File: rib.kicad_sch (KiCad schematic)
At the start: 92 parts, among them J1 RJ45_LED, J10 Conn_01x04_Male, J11 Screw_Terminal_01x02, J12 Screw_Terminal_01x02, J13 Screw_Terminal_01x02, J14 Conn_01x02_Male, J15 Conn_01x02_Male, J16 Conn_01x06_Male, J2 RJ45_LED, J3 RJ45_LED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

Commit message: Fix xbee connection visuals
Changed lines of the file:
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@@
-    (stroke (width 0) (type default))
-  )
-  (wire (pts (xy 289.56 44.45) (xy 326.39 44.45))
     (stroke (width 0) (type default))
   )
@@
   )
   (wire (pts (xy 129.54 246.38) (xy 129.54 248.92))
-    (stroke (width 0) (type default))
-  )
-  (wire (pts (xy 289.56 67.31) (xy 326.39 67.31))
     (stroke (width 0) (type default))
   )
@@
     )
   )
-  (global_label "3.3V" (shape input) (at 326.39 44.45 180) (fields_autoplaced)
-    (effects (font (size 1.27 1.27)) (justify right))
-    (property "Intersheetrefs" "${INTERSHEET_REFS}" (at 319.8645 44.3706 0)
+  (global_label "3.3V" (shape input) (at 289.56 44.45 180) (fields_autoplaced)
+    (effects (font (size 1.27 1.27)) (justify right))
+    (property "Intersheetrefs" "${INTERSHEET_REFS}" (at 283.0345 44.3706 0)
       (effects (font (size 1.27 1.27)) (justify right) hide)
     )
@@
     )
   )
-  (symbol (lib_id "power:GND") (at 326.39 67.31 270) (unit 1)
+  (symbol (lib_id "power:GND") (at 289.56 67.31 270) (unit 1)
     (in_bom yes) (on_board yes) (dnp no)
-    (property "Reference" "#PWR0138" (at 320.04 67.31 0)
-      (effects (font (size 1.27 1.27)) hide)
-    )
-    (property "Value" "GND" (at 318.77 67.31 90)
+    (property "Reference" "#PWR0138" (at 283.21 67.31 0)
+      (effects (font (size 1.27 1.27)) hide)
+    )
+    (property "Value" "GND" (at 281.94 67.31 90)
       (effects (font (size 1.27 1.27)) (justify left))
     )
-    (property "Footprint" "" (at 326.39 67.31 0)
-      (effects (font (size 1.27 1.27)) hide)
-    )
-    (property "Datasheet" "" (at 326.39 67.31 0)
-      (effects (font (size 1.27 1.27)) hide)
-    )
+    (property "Footprint" "" (at 289.56 67.31 0)
+      (effects (font (size 1.27 1.27)) hide)
+    )
+    (property "Datasheet" "" (at 289.56 67.31 0)
+      (effects (font (size 1.27 1.27)) hide)
+    )

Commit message: Fix issues with RC1 - LED orientation, pullups, 3v3 source
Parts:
- added C8: 33uF, Capacitor_THT:CP_Radial_D5.0mm_P2.50mm, symbol Device:C_Polarized
- added U10: LM3940IT-3.3, Package_TO_SOT_THT:TO-220-3_Vertical, symbol LM3940:LM3940IT-3.3
- RN1: value R_Network06 -> 10k_Network06; R 10k -> (none)
- RN2, RN3, RN4: value R_Network05 -> 2k_Network05; R 2k -> (none)
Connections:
- net 3.3V: now also R38.2, R39.2, C8.1, U10.3 (OUT); no longer U1.36 (3V3)
- net 5V: now also R37.1, U10.1 (IN)
- net CATHODE3: now also J1.11, J1.9, J2.11, J2.9, J3.11, J3.9, J4.11, J4.9; no longer J1.10, J1.12, J2.10, J2.12, J3.10, J3.12, J4.10, J4.12
- net GND: now also C8.2, U10.2 (GND); no longer R37.1, R38.2, R39.2
- net LED1: now also J1.12; no longer J1.11
- net LED2: now also J1.10; no longer J1.9
- net LED3: now also J2.12; no longer J2.11
- net LED4: now also J2.10; no longer J2.9
- net LED5: now also J3.12; no longer J3.11
- net LED6: now also J3.10; no longer J3.9
- net LED7: now also J4.12; no longer J4.11
- net LED8: now also J4.10; no longer J4.9
- net MOSFET1: now reaches D6.2 (A), J12.2 (Pin_2), Q1.2 (D)
- net MOSFET2: now reaches D7.2 (A), J13.2 (Pin_2), Q2.2 (D)
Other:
- note removed: "Pullup and enable after not floating"

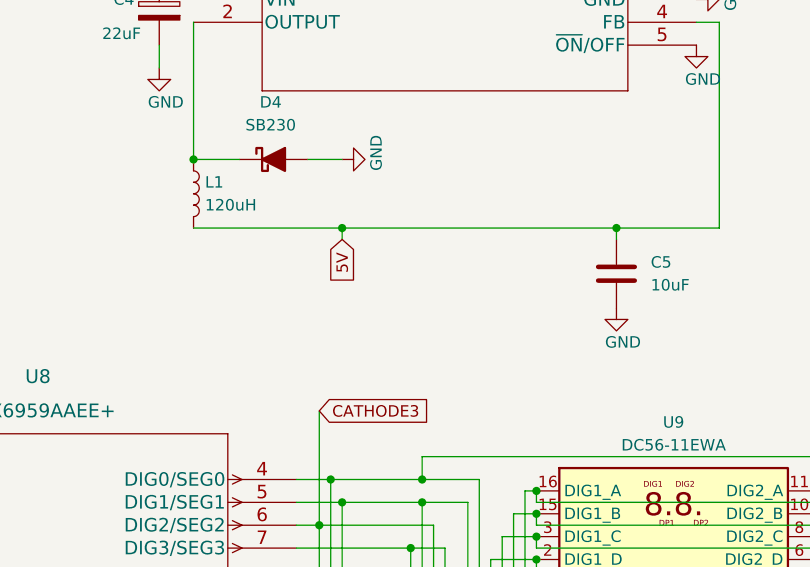
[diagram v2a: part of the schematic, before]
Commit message: prepare to add zener diode
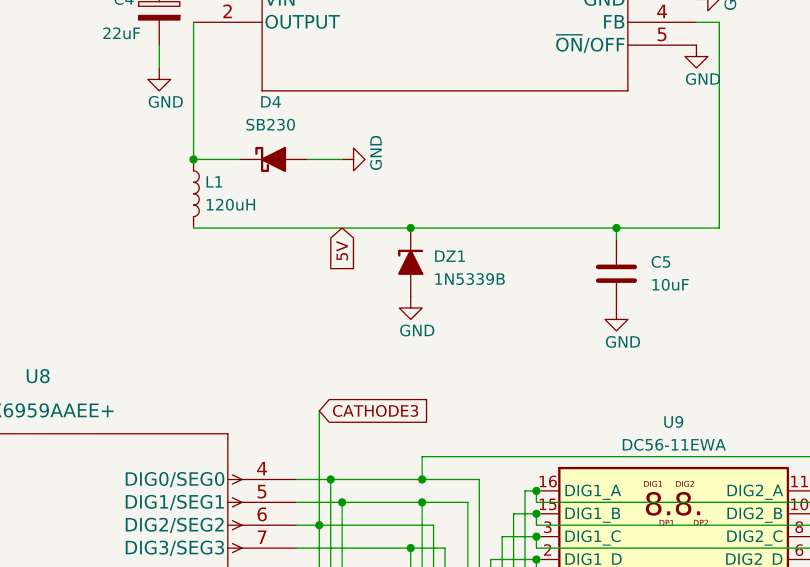
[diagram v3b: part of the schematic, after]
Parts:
- added DZ1: 1N5339B, Diode_THT_AKL:D_5W_CASE-017AA_P12.70mm_Horizontal_Zener, symbol Diode_Zener_AKL:1N5339B
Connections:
- net 5V: now also DZ1.1 (K)
- net GND: now also DZ1.2 (A)
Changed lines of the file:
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@@
   (junction (at 358.14 177.8) (diameter 0) (color 0 0 0 0)
   )
-  (junction (at 351.79 118.11) (diameter 0) (color 0 0 0 0)
-  )
   (junction (at 373.38 147.32) (diameter 0) (color 0 0 0 0)
   )
@@
   (junction (at 355.6 168.91) (diameter 0) (color 0 0 0 0)
   )
+  (junction (at 359.41 118.11) (diameter 0) (color 0 0 0 0)
+  )
   (junction (at 259.08 160.02) (diameter 0) (color 0 0 0 0)
   )
@@
     (stroke (width 0) (type default))
   )
+  (wire (pts (xy 335.28 118.11) (xy 359.41 118.11))
+    (stroke (width 0) (type default))
+  )
   (wire (pts (xy 85.09 20.32) (xy 85.09 87.63))
     (stroke (width 0) (type default))
@@
     (stroke (width 0) (type default))
   )
-  (wire (pts (xy 335.28 118.11) (xy 351.79 118.11))
-    (stroke (width 0) (type default))
-  )
   (wire (pts (xy 236.22 157.48) (xy 246.38 157.48))
     (stroke (width 0) (type default))
@@
     (stroke (width 0) (type default))
   )
+  (wire (pts (xy 359.41 118.11) (xy 382.27 118.11))
+    (stroke (width 0) (type default))
+  )
   (wire (pts (xy 363.22 153.67) (xy 359.41 153.67))
     (stroke (width 0) (type default))
@@
     (stroke (width 0) (type default))
   )
-  (wire (pts (xy 351.79 118.11) (xy 351.79 119.38))
-    (stroke (width 0) (type default))
-  )
   (wire (pts (xy 33.02 52.07) (xy 33.02 34.29))
     (stroke (width 0) (type default))
@@
     (stroke (width 0) (type default))
   )
-  (wire (pts (xy 351.79 118.11) (xy 382.27 118.11))
-    (stroke (width 0) (type default))
-  )
   (wire (pts (xy 71.12 234.95) (xy 81.28 234.95))
     (stroke (width 0) (type default))
@@
     )
   )
-  (global_label "5V" (shape input) (at 351.79 119.38 270) (fields_autoplaced)
+  (global_label "5V" (shape input) (at 351.79 118.11 270) (fields_autoplaced)
     (effects (font (size 1.27 1.27)) (justify right))
-    (property "Intersheetrefs" "${INTERSHEET_REFS}" (at 351.8694 124.0912 90)
+    (property "Intersheetrefs" "${INTERSHEET_REFS}" (at 351.8694 122.8212 90)
       (effects (font (size 1.27 1.27)) (justify right) hide)
     )
@@
     )
   )
+  (symbol (lib_id "power:GND") (at 359.41 125.73 0) (unit 1)
+    (in_bom yes) (on_board yes) (dnp no)
+    (property "Reference" "#PWR09" (at 359.41 132.08 0)
+      (effects (font (size 1.27 1.27)) hide)
+    )
+    (property "Value" "GND" (at 358.14 129.54 0)
+      (effects (font (size 1.27 1.27)) (justify left))
+    )
+    (property "Footprint" "" (at 359.41 125.73 0)
+      (effects (font (size 1.27 1.27)) hide)
+    )
+    (property "Datasheet" "" (at 359.41 125.73 0)
+      (effects (font (size 1.27 1.27)) hide)
+    )
+    (pin "1")
+    (instances
+      (project "rib"
+        (path "/33b057c3-d7c8-4264-8eb6-c3b5e9165be1"
+          (reference "#PWR09") (unit 1)
+        )
+      )
+    )
+  )
   (symbol (lib_id "power:GND") (at 129.54 217.17 270) (unit 1)
     (in_bom yes) (on_board yes) (dnp no) (fields_autoplaced)
@@
         )
       )
+    )
+  )
+  (symbol (lib_id "Diode_Zener_AKL:1N5339B") (at 359.41 121.92 90) (unit 1)
+    (in_bom yes) (on_board yes) (dnp no) (fields_autoplaced)
+    (property "Reference" "DZ1" (at 361.95 121.285 90)
+      (effects (font (size 1.27 1.27)) (justify right))
+    )
+    (property "Value" "1N5339B" (at 361.95 123.825 90)
+      (effects (font (size 1.27 1.27)) (justify right))
+    )
+    (property "Footprint" "Diode_THT_AKL:D_5W_CASE-017AA_P12.70mm_Horizontal_Zener" (at 359.41 121.92 0)
+      (effects (font (size 1.27 1.27)) hide)
+    )
+    (property "Datasheet" "https://www.tme.eu/Document/56402a6b26bc9a1a5ede882b3d258cff/1N53_ser.pdf" (at 359.41 121.92 0)
+      (effects (font (size 1.27 1.27)) hide)
+    )
+    (pin "1")
+    (pin "2")
+    (instances
+      (project "rib"
+        (path "/33b057c3-d7c8-4264-8eb6-c3b5e9165be1"
+          (reference "DZ1") (unit 1)
+        )
+      )

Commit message: v1.0 design update (BOMs not updated)
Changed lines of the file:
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@@
     )
     (property "Footprint" "Capacitor_THT:CP_Radial_D5.0mm_P2.50mm" (at 332.4352 97.79 0)
-      (effects (font (size 1.27 1.27)) hide)
+      (effects (font (size 1.27 1.27)))
     )
     (property "Datasheet" "~" (at 331.47 93.98 0)

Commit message: RIB v1.1 pre-release, documentation
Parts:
- removed J7: Conn_01x02_Male, Connector_PinHeader_2.54mm:PinHeader_1x02_P2.54mm_Vertical, symbol Connector:Conn_01x02_Male
- removed R35, R36: 10k, Resistor_THT:R_Axial_DIN0207_L6.3mm_D2.5mm_P10.16mm_Horizontal, symbol Device:R
- removed RN1: 10k_Network06, Resistor_THT:R_Array_SIP7, symbol Device:R_Network06
- added J17, J18, J19: Conn_01x02_Male, Connector_PinHeader_2.54mm:PinHeader_1x02_P2.54mm_Vertical, symbol Connector:Conn_01x02_Male
- added J7: Conn_01x04_Male, Connector_PinHeader_2.54mm:PinHeader_1x04_P2.54mm_Vertical, symbol Connector:Conn_01x04_Male
- added RN1: R_Network08, Resistor_THT:R_Array_SIP9, symbol Device:R_Network08
- C6, C7: value 1uF -> 10uF
- R40, R41: value 33k -> 10k
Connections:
- net 3.3V: now also J18.1 (Pin_1), J19.1 (Pin_1), RN1.1 (common)
- net GND: now also J18.2 (Pin_2), J19.2 (Pin_2); no longer J3.6, J4.6
- net at J4.3, U1.24 (GPIO18): now also RN1.9 (R8)
- net at J4.4, U1.25 (GPIO19): now also RN1.8 (R7)
- net at J4.5: now also J7.3 (Pin_3), RN1.7 (R6)
- net at J3.5: now also J7.1 (Pin_1), RN1.4 (R3)
- net at J3.4, U1.20 (GPIO15): now also RN1.5 (R4)
- net at J3.3, U1.19 (GPIO14): now also RN1.6 (R5)
- net at U7.13 (~{INT}): now also J17.1 (Pin_1)
- net at U6.13 (~{INT}): now also J17.2 (Pin_2)
- new net: J3.6, J7.2 (Pin_2), RN1.2 (R1)
- new net: J4.6, J7.4 (Pin_4), RN1.3 (R2)
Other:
- note added: "09/25/2023"
- note added: "3 Extra GPIO"
- note added: "5v to 3v3"
- note added: "8-60v to 5v"
- note added: "Addr 0x20"
- note added: "Addr 0x21"
- note added: "Addr 0x38"
- note added: "Breakout of EX1/EX2 with pullups"
- note added: "EX2"
- note added: "I/O Expanders"
- note added: "I2C"
- note added: "Illinois Tech Robotics Robot Interface Board (RIB)"
- note added: "Interrupt connections breakout"
- note added: "LED driver circuitry"
- note added: "Orange/EX1"
- note added: "Power connections"
- note added: "Reset button"
- note added: "Select between VIN or VOUT 3v3, 5, VIN for Optocoupler voltage"
- note added: "v1.1"
- note removed: "Orange"
- moved on the sheet: C6, C7, J3, J4, R38, R39
